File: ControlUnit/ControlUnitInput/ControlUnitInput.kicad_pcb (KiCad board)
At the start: 2 copper layers, 101.1 x 90 mm, 43 parts, among them SW1 SW_Push, SW10 SW_Push, SW11 SW_Push, SW13 SW_Push, SW14 SW_Push, SW15 SW_Push, SW16 SW_Push, SW2 SW_Push, SW3 SW_Push, SW4 SW_Push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

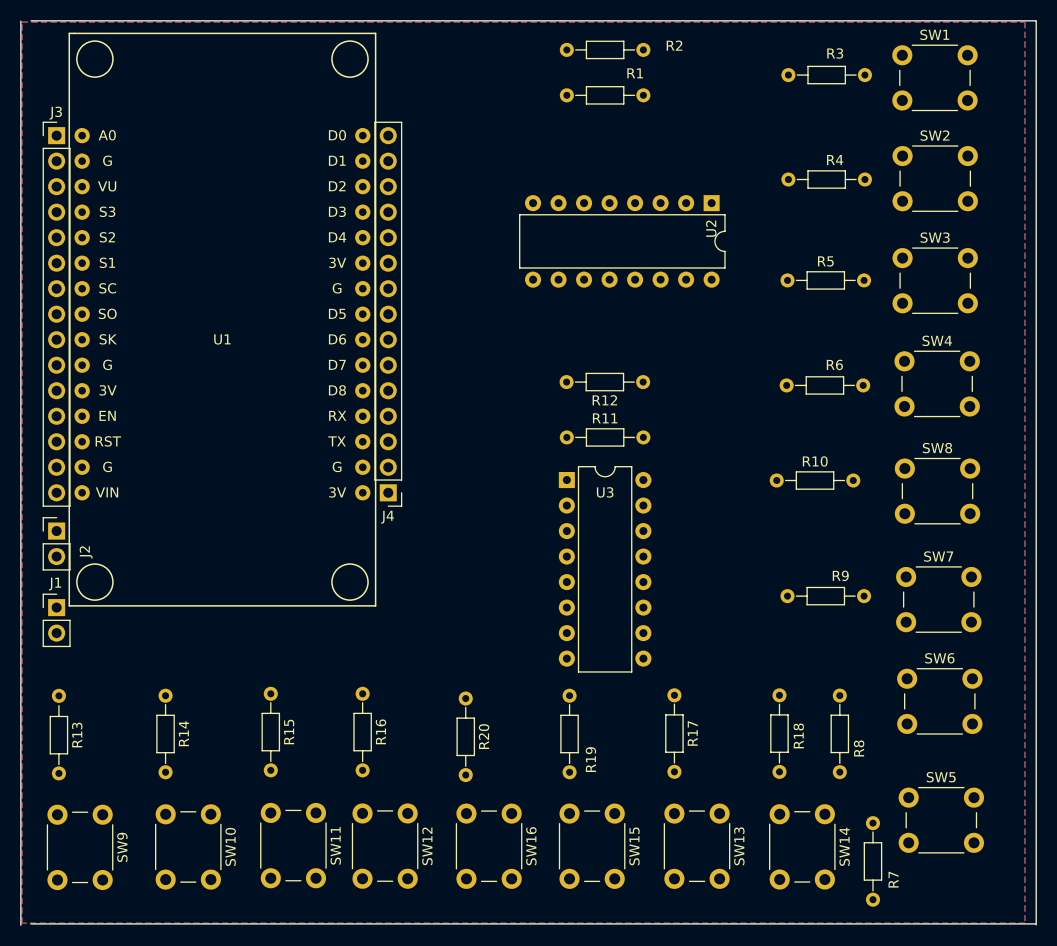
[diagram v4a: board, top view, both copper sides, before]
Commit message: Revert "realign components and fix track widths"
This reverts commit 8eef0b6b7679f1414a0b9c1d3560c4b6c89cb1c1.
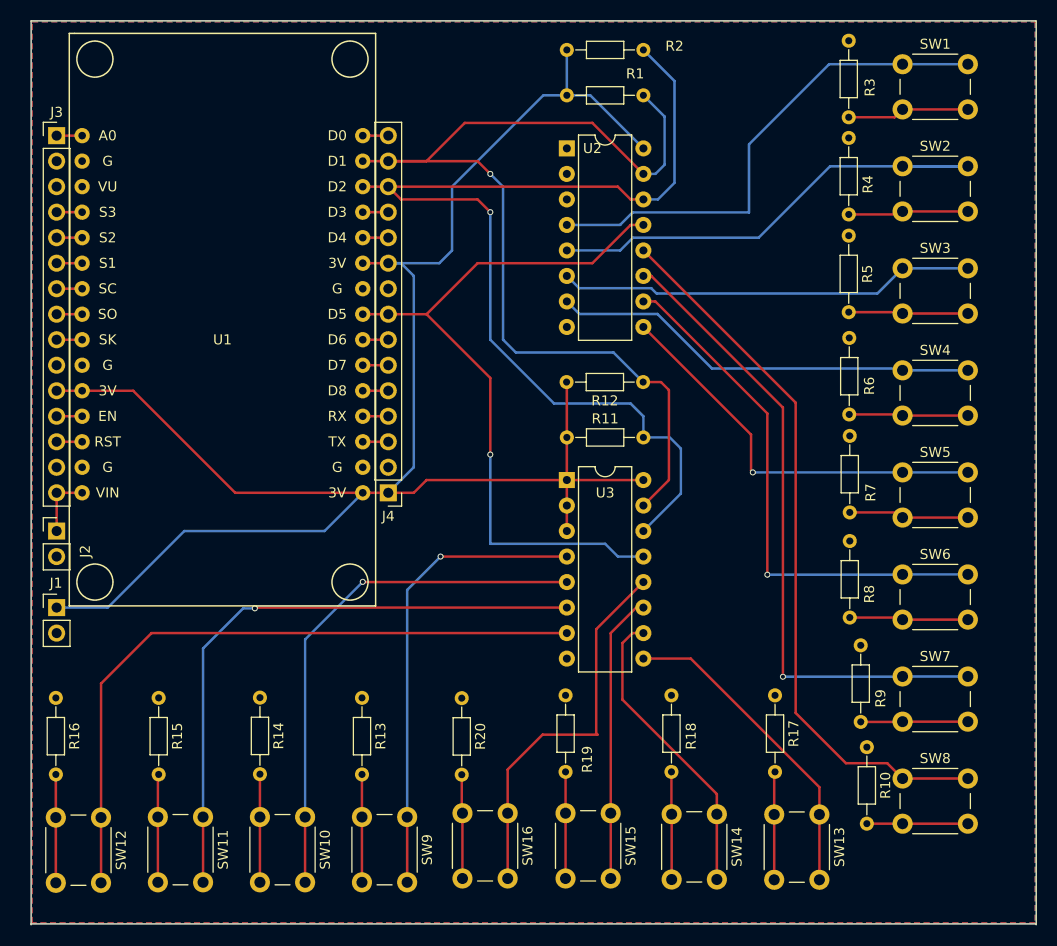
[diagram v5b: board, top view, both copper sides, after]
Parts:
- moved R7 38.6 mm to (94.2, 54.0)
- moved SW5 32.4 mm to (99.5, 57.7)
- moved SW8 30.9 mm to (99.5, 88.1)
- moved R16 30.5 mm to (15.2, 80.1)
- moved SW12 30.5 mm to (19.7, 92.0)
- moved SW9 30.3 mm to (50.1, 92.0)
- moved R13 30.2 mm to (45.6, 80.1)
- moved R10 28.0 mm to (95.9, 85.0), turned to 270 degrees
- moved R8 15.4 mm to (94.2, 64.5)
- moved U2 15.4 mm to (66.0, 25.4), turned to 0 degrees
- moved SW11 11.3 mm to (29.8, 92.0)
- moved R15 11.2 mm to (25.4, 80.1)
- moved R18 10.8 mm to (76.5, 79.9)
- moved SW14 10.8 mm to (81.0, 91.7)
- moved SW6 10.4 mm to (99.5, 67.8)
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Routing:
- net +3V3: track 0.00 -> 184.2 mm
- net SCL: track 0.00 -> 105.1 mm, vias 0 -> 1
- net SDA: track 0.00 -> 101.4 mm, vias 0 -> 1
- net INT: track 0.00 -> 73.2 mm, vias 0 -> 1
- net Net-(SW8-Pad1): track 0.00 -> 72.2 mm
- net Net-(SW12-Pad1): track 0.00 -> 68.3 mm
- net Net-(SW7-Pad1): track 0.00 -> 64.5 mm, vias 0 -> 1
- net Net-(SW11-Pad1): track 0.00 -> 61.2 mm, vias 0 -> 1
- net Net-(SW6-Pad1): track 0.00 -> 53.0 mm, vias 0 -> 1
- net Net-(SW10-Pad1): track 0.00 -> 52.6 mm, vias 0 -> 1
- net Net-(SW1-Pad1): track 0.00 -> 50.5 mm
- net Net-(SW2-Pad1): track 0.00 -> 49.9 mm
- net Net-(SW9-Pad1): track 0.00 -> 46.4 mm, vias 0 -> 1
- net Net-(SW4-Pad1): track 0.00 -> 42.8 mm
- net Net-(SW3-Pad1): track 0.00 -> 41.7 mm
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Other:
- board size 101.1 x 90 mm -> 100.1 x 90 mm
- net class Default: clearance 0.3 -> 0.2; trace_width 0.5 -> 0.25; via_dia 0.8 -> 0.6
- rule trace_clearance: 0.3 -> 0.2
- board text added: "Rev 0.2"
- board text removed: "Rev 0.3"
